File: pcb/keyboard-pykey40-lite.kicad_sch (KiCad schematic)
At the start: 135 parts, among them J1 USB_C_Receptacle_USB2.0, J2 Conn_01x03, U1 RP2040, U2 W25Q128JVS, U3 USBLC6-2SC6, U4 AMS1117-3.3, Y1 12MHz

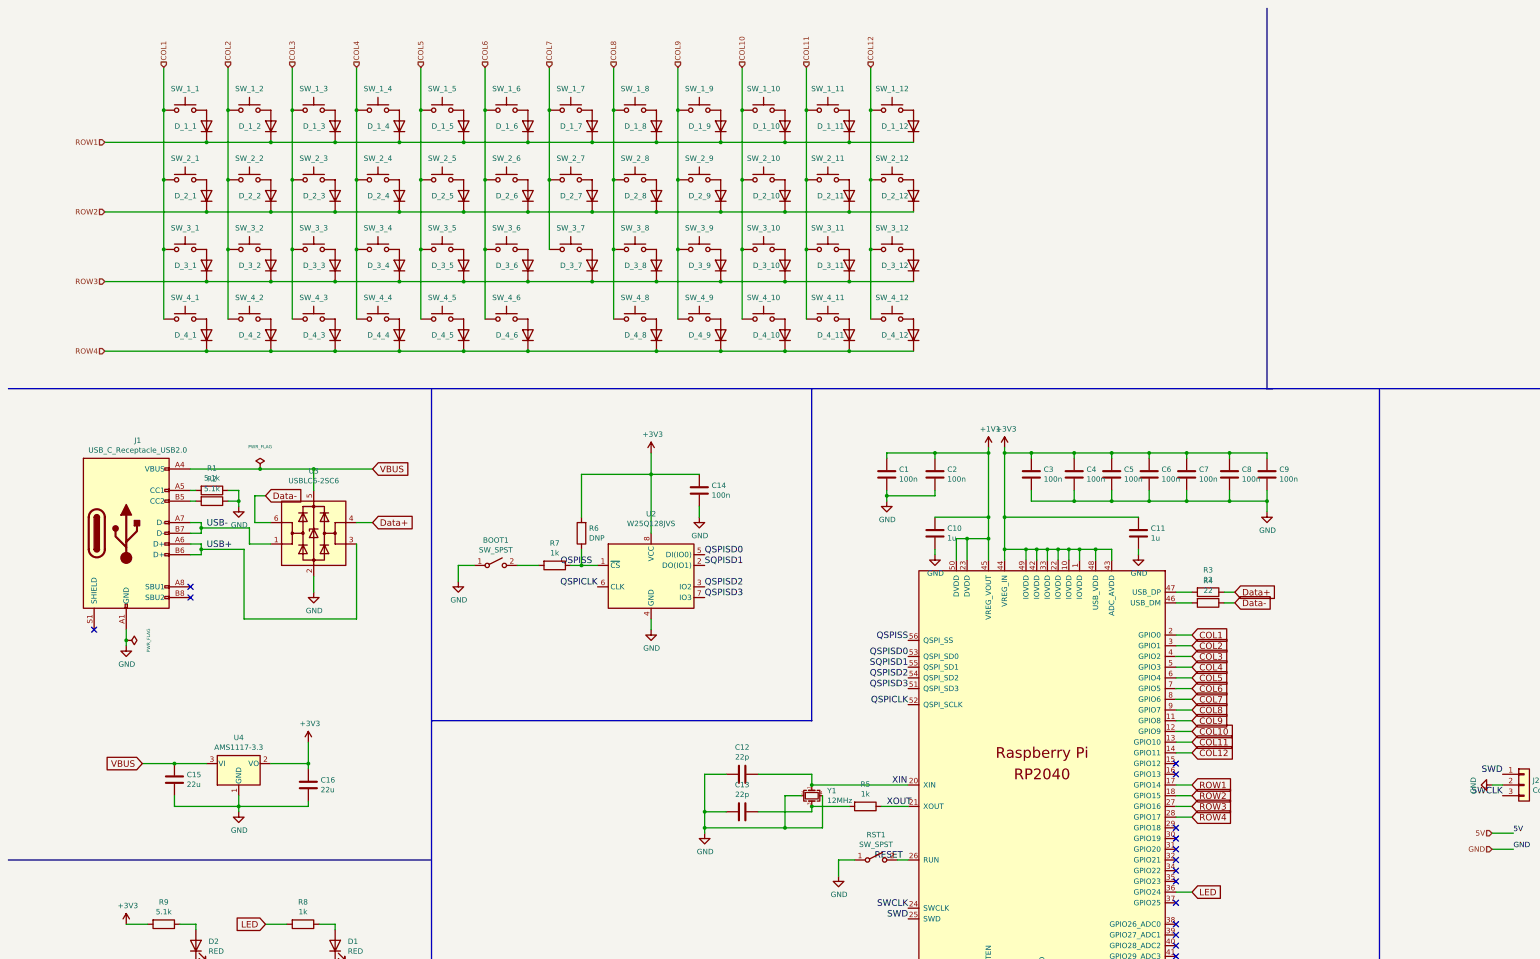
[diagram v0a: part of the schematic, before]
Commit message: pcb: add text to schematic keyboard-pykey40-lite
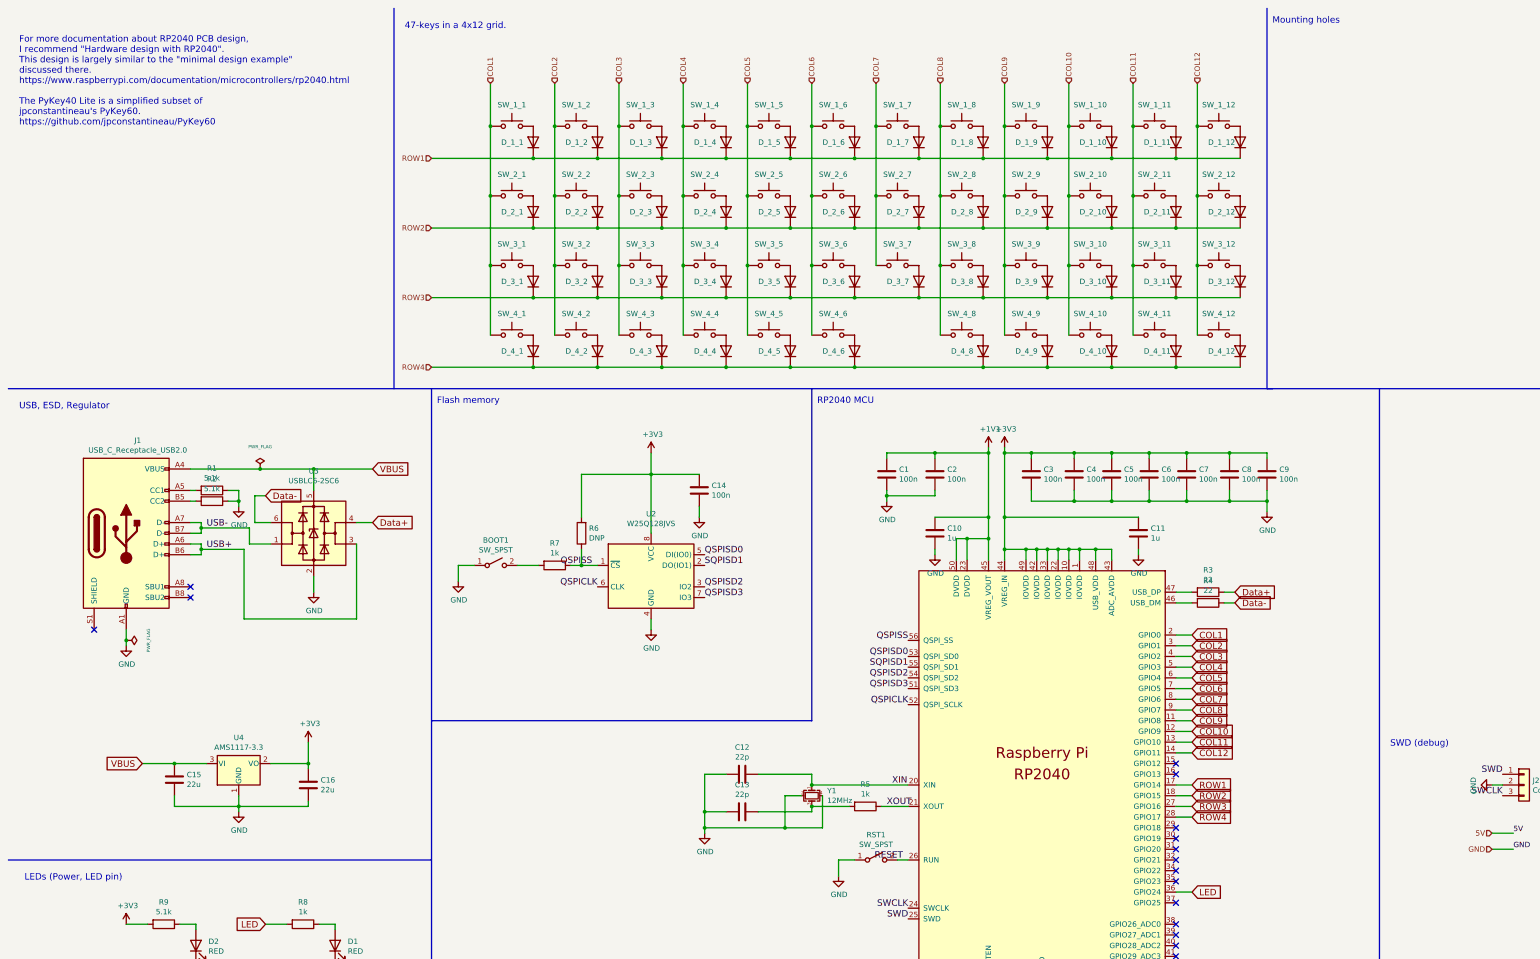
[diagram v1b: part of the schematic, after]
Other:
- note added: "47-keys in a 4x12 grid."
- note added: "Flash memory"
- note added: "For more documentation about RP2040 PCB design, I recommend "Hardware design with RP2040". This design is largely similar to the "minimal design example" discussed there. https://www.raspberrypi.com/documentation/microcontrollers/rp2040.html The PyKey40 Lite is a simplified subset of jpconstantineau's PyKey60. https://github.com/jpconstantineau/PyKey60"
- note added: "LEDs (Power, LED pin)"
- note added: "Mounting holes"
- note added: "RP2040 MCU"
- note added: "SWD (debug)"
- note added: "USB, ESD, Regulator"
- moved on the sheet: D_1_1, D_1_10, D_1_11, D_1_12, D_1_2, D_1_3, D_1_4, D_1_5, D_1_6, D_1_7, D_1_8, D_1_9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
